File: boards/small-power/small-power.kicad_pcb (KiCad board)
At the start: 2 copper layers, 100 x 45 mm, 31 parts, among them J1 Conn_01x02_Female, J2 Conn_01x02_Female, J3 Conn_01x02_Female, J4 Conn_01x02_Female, J5 Conn_01x02_Female, M1 MountingHole_3mm, M2 MountingHole_3mm, M3 MountingHole_3mm, M4 MountingHole_3mm, Q1 TIP3055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

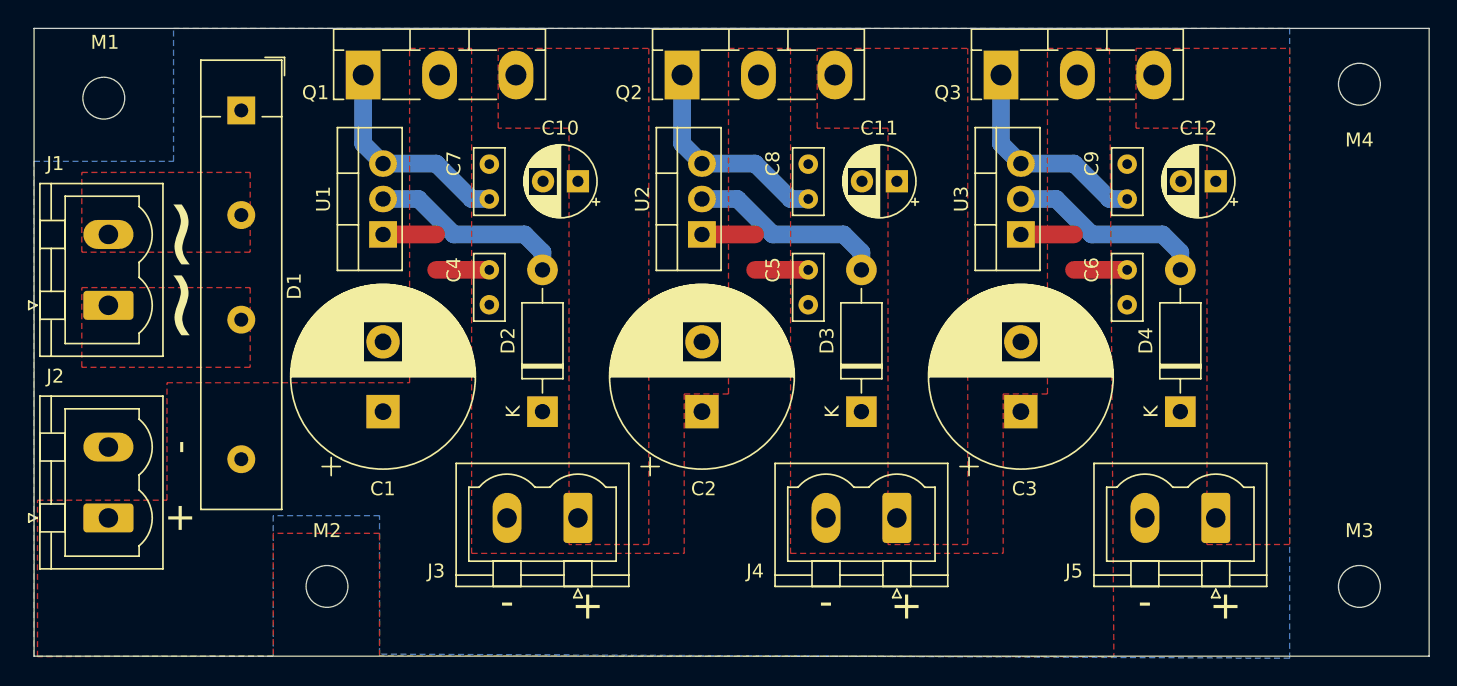
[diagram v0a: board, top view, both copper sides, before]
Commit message: small-power: updated to kicad 7
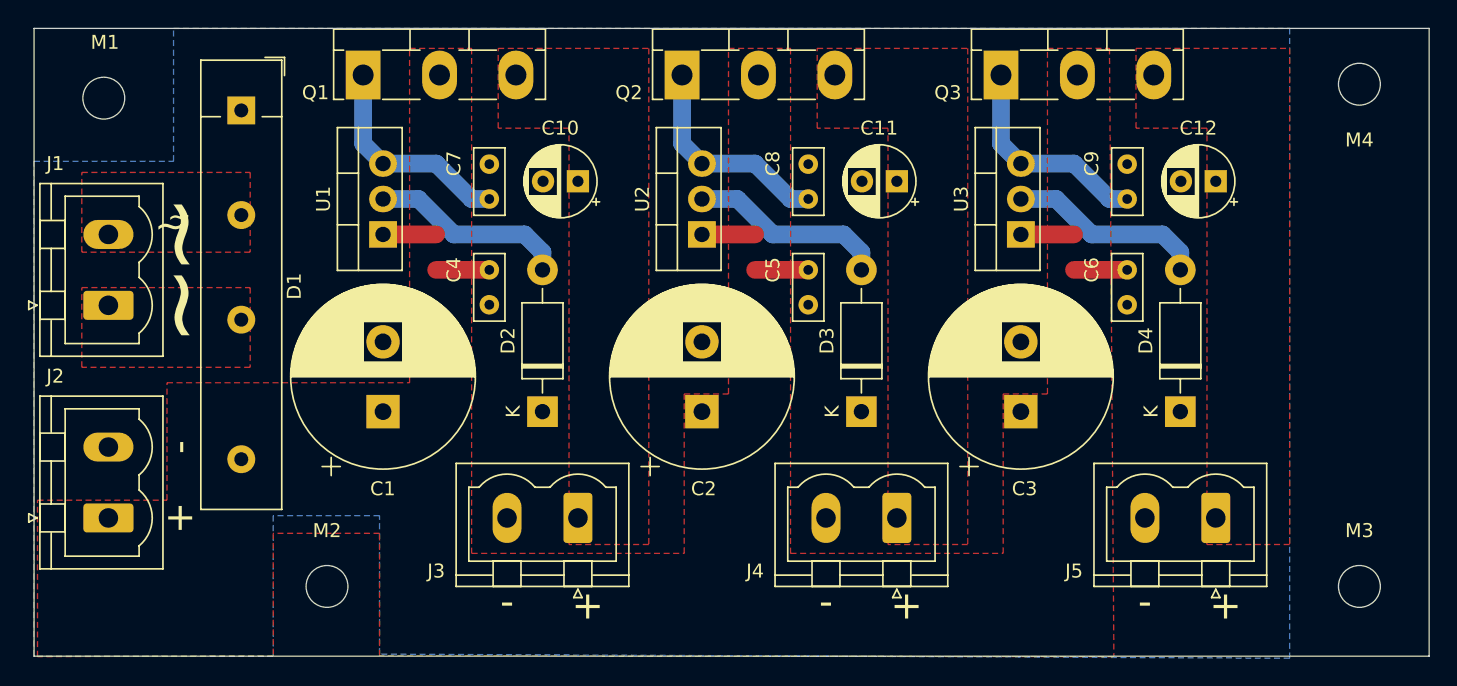
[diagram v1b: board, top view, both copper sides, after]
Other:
- net class Default removed
- board text removed: "~~"
